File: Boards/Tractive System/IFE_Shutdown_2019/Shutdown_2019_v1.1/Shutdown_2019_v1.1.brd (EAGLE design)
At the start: 88.9 x 76.2 mm, 195 parts, among them Q1 DMN6140L-7, Q10 DMN6140L-7, Q11 DMP3099L-7, Q12 IRLML6346PBF, Q13 IRLML6346PBF, Q14 IRLML6346PBF, Q15 DMP3099L-7, Q16 DMN6140L-7, Q17 IRLML6346PBF, Q18 DMN6140L-7, Q2 DMN6140L-7, Q20 DMN6140L-7, Q21 DMN6140L-7, Q3 DMN6140L-7, Q4 DMN6140L-7, Q5 DMN6140L-7, Q6 DMP3099L-7, Q7 DMN6140L-7, Q9 DMN6140L-7, U1 STM32F103CBT6, U2 STM32F103CBT6

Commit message: Still working on 1.1
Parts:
- removed BUZZER: PKMCS0909E4000, MURATA:PKMCS
- added U$6: MAS806Q, MALLORY:MAS806Q
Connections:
- net +12V: now also U$6.POS; no longer BUZZER.P$1
- net N$4: now also U$6.NEG; no longer BUZZER.P$2
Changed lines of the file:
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@@
 <?xml version="1.0" encoding="utf-8"?>
 <!DOCTYPE eagle SYSTEM "eagle.dtd">
-<eagle version="9.2.2">
+<eagle version="9.1.2">
 <drawing>
 <settings>
@@
 <attribute name="NAME" x="22.225" y="26.797" size="0.8128" layer="25" rot="R180"/>
 </element>
-<element name="BUZZER" library="MURATA" package="PKMCS" value="PKMCS0909E4000" x="94.742" y="18.796" smashed="yes" rot="R90">
-<attribute name="NAME" x="89.789" y="14.224" size="0.8128" layer="25" rot="R90"/>
-</element>
 <element name="U$1" library="KEMET" package="DPDT_2.54" value="EC2" x="16.51" y="67.31" smashed="yes" rot="R90">
 <attribute name="NAME" x="20.574" y="74.676" size="0.8128" layer="25" rot="R270"/>
@@
 <attribute name="NAME" x="40.894" y="74.676" size="0.8128" layer="25" rot="R270"/>
 </element>
+<element name="U$6" library="MALLORY" package="MAS806Q" value="MAS806Q" x="104.902" y="29.972" rot="R180"/>
 </elements>
 <signals>
@@
 <wire x1="14.7546" y1="64.77" x2="17.46" y2="64.77" width="0.4064" layer="16"/>
 <wire x1="15.748" y1="45.5372" x2="15.748" y2="49.53" width="0.4064" layer="1"/>
-<contactref element="BUZZER" pad="P$1"/>
 <contactref element="U$1" pad="$P5"/>
 <contactref element="U$2" pad="$P5"/>
 <contactref element="U$3" pad="$P5"/>
-<wire x1="94.742" y1="14.296" x2="16.256" y2="45.0292" width="0" layer="19" extent="1-1"/>
-<wire x1="19.05" y1="71.12" x2="94.742" y2="14.296" width="0" layer="19" extent="1-1"/>
-<wire x1="29.21" y1="71.12" x2="19.05" y2="71.12" width="0" layer="19" extent="1-1"/>
-<wire x1="39.37" y1="71.12" x2="29.21" y2="71.12" width="0" layer="19" extent="1-1"/>
+<contactref element="U$6" pad="POS"/>
+<wire x1="37.78" y1="67.63" x2="39.37" y2="71.12" width="0" layer="19" extent="16-16"/>
+<wire x1="29.21" y1="71.12" x2="27.62" y2="67.63" width="0" layer="19" extent="16-16"/>
+<wire x1="19.05" y1="71.12" x2="17.46" y2="67.63" width="0" layer="19" extent="16-16"/>
+<wire x1="104.902" y1="36.972" x2="16.256" y2="45.0292" width="0" layer="19" extent="1-1"/>
 </signal>
 <signal name="FAULT_BSPD_STAT">
@@
 </signal>
 <signal name="N$4">
-<contactref element="BUZZER" pad="P$2"/>
 <contactref element="Q4" pad="3"/>
-<wire x1="94.742" y1="23.296" x2="86.36" y2="16.34" width="0" layer="19" extent="1-1"/>
+<contactref element="U$6" pad="NEG"/>
+<wire x1="104.902" y1="22.972" x2="86.36" y2="16.34" width="0" layer="19" extent="1-1"/>
 </signal>
 <signal name="ANALOG_5V" class="1">

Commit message: Finished pre review Safety V1.1
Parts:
- removed CURRENT_SENSOR_SUPPLY, PWR: MINIFIT_JR_5566-02, Display_Custom:MINIFIT_JR_5566-02
- removed DRIVERS, FAULT_INPUT, HALL_SENSE, THROTTLE, TSAL_EN: MINIFIT_JR_5566-04, Display_Custom:MINIFIT_JR_5566-04
- removed Q17: IRLML6346PBF, TRANS:SOT23
- removed R6: 3.6k, rcl:R0603
- added C40, C41: 0.001u, rcl:C0805
- added C42, C43, C44, C45, C46: 0.1u, resistor:C0603
- added CURRENT_SENSE_SUPPLY, POWER, POWER_ANALOG, SOFT_FAULT_STAT: 505575-02, MOLEX:505575-02
- added FAULT_IN, LIGHTING, THROTTLE_TC: 505575-05, MOLEX:505575-05
- added FAULT_STAT: 505575-03, MOLEX:505575-03
- added HALL_SENSOR_INPUT: 505575-04, MOLEX:505575-04
- added Q8: DMN6140L-7, TRANS:SOT23
- added R10, R78: 10, rcl:R0603
- added R45, R75, R79, R80: 10k, rcl:R0603
- added R76, R81: 15k, rcl:R0603
- added R77, R82: 1k, rcl:R0603
- added R83: 10k, resistor:R0603
- added U$13, U$15: LMV321L, STM:SOT23-5
- added U$14, U$19: BZT52C5V6, DIODES_INC:SOD-123
- added U$27: SN74LVC1G08, TEXAS_INSTRUMENTS:SOT23-5
- added U$28: CD4072BM96, TEXAS_INSTRUMENTS:SOIC8
- added U$30, U$31: TS881, STM:SOT23-5
- AIR, CAN, ENABLE: value MINIFIT_JR_5566-02 -> 505575-02; device Display_Custom:MINIFIT_JR_5566-02 -> MOLEX:505575-02
- Q13: value IRLML6346PBF -> DMN6140L-7
- R3: value 3.6k -> 10k; device rcl:R0603 -> resistor:R0603
- U$7: value DNBT8105 -> SN74LVC1G04DBVR; device DIODES_INC:SOT23-3 -> Display_Custom:SOT23-5L
- U$8: value DNBT8105 -> 0805_INDUCTOR; device DIODES_INC:SOT23-3 -> Display_Custom:L0805
- moved U$8 275.9 mm to (-52.8, -227.3), turned to 0 degrees
- moved R3 274.2 mm to (-53.6, -222.5)
- moved Q13 272.2 mm to (-47.0, -216.4), turned to 0 degrees
- moved U$7 271.9 mm to (-52.6, -216.7), turned to 0 degrees
- moved Q4 57.5 mm to (45.7, 55.9)
- moved C11 47.2 mm to (99.3, 82.8), turned to 90 degrees
- moved C14 47.2 mm to (99.3, 87.9), turned to 270 degrees
- moved FUSE 45.0 mm to (80.3, 93.0)
- moved D11 44.3 mm to (97.3, 82.8), turned to 0 degrees
- moved D12 44.3 mm to (97.3, 87.9), turned to 180 degrees
- moved U$25 43.4 mm to (4.06, 79.8)
- moved C22 43.0 mm to (3.30, 76.2)
- moved R25 42.9 mm to (3.81, 72.9)
- moved R33 42.4 mm to (6.86, 77.5)
- moved R34 42.3 mm to (6.86, 75.2)
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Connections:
- removed net BSPD_OC: Q17.1, U$17.1
- removed net BSPD_SC: Q14.1, U$16.1
- removed net N$15: R3.2, U$8.1
- removed net N$16: R6.2, U$7.1
- removed net TSAL_HV_EN: R3.1, U1.22
- removed net TSAL_LV_EN: R6.1, U1.25
- new net APPS_STAT: SOFT_FAULT_STAT.1
- new net BRAKE_POS: R10.1, THROTTLE_TC.5
- new net BRAKE_POS_F: R75.2, U$13.3, U$13.4
- new net BRAKE_POS_F_3_3: R75.1, R76.2, U1.11
- new net BSPD_BP_OC: U$28.P2, U$31.1
- new net BSPD_BP_SC: U$28.P3, U$30.1
- new net BSPD_COND: Q12.1, R83.2, U$27.4
- new net BSPD_CS_OC: U$17.1, U$28.P4
- new net BSPD_CS_SC: U$16.1, U$28.P5
- new net BSPD_SENSOR_FAULT: Q14.1, U$28.P1
- new net BTSF_STAT: SOFT_FAULT_STAT.2
- new net N$22: R78.2, R79.1, R82.1, U$19.C
- new net N$23: C41.1, R79.2, U$15.1
- new net N$5: R10.2, R45.1, R77.1, U$14.C
- new net N$7: C40.1, R45.2, U$13.1
- new net STEERING_POS: R78.1, THROTTLE_TC.4
- new net STEERING_POS_F: R80.2, U$15.3, U$15.4
- new net STEERING_POS_F_3_3: R80.1, R81.2, U1.12
- net +3V3: now also U$7.5
- net +5V: now also C42.1, C43.1, C44.1, C45.1, C46.1, CURRENT_SENSE_SUPPLY.1, R77.2, R82.2, U$13.5, U$15.5, U$27.5, U$28.P14, U$30.5, U$31.5; no longer CURRENT_SENSOR_SUPPLY.1, TSAL_EN.1
- net AGND: now also POWER_ANALOG.2, U$8.1
- net AIR_IN: now also AIR.2; no longer AIR.1
- net AIR_OUT: now also AIR.1; no longer AIR.2
- net ANALOG_5V: now also POWER_ANALOG.1
- net BRAKE_LIGHT-: now also LIGHTING.4; no longer DRIVERS.1
- net BRAKE_PRESSURE: now also FAULT_IN.4; no longer FAULT_INPUT.4
- net BRAKE_PRESSURE_F: now also U$30.4, U$31.3
- net BSPD_BRAKE_COND: now also U$27.2; no longer Q13.1
- net BSPD_CURR_COND: now also U$27.1; no longer Q12.1
- net CURRENT_SENSE: now also FAULT_IN.5; no longer FAULT_INPUT.2
- net ENABLE_IN: now also ENABLE.2; no longer ENABLE.1
- net ENABLE_OUT: now also ENABLE.1; no longer ENABLE.2
- net FAULT_BMS: now also FAULT_IN.3; no longer FAULT_INPUT.1
- net FAULT_BMS_STAT: now also FAULT_STAT.2
- net FAULT_BMS_STATUS_3_3: now also U1.22; no longer U1.12
- net FAULT_BSPD: no longer Q17.3
- net FAULT_BSPD_STAT: now also FAULT_STAT.1
- net FAULT_IMD: now also FAULT_IN.2; no longer FAULT_INPUT.3
- net FAULT_IMD_STAT: now also FAULT_STAT.3
- net FAULT_RESET: now also FAULT_IN.1; no longer TSAL_EN.4
- net GND: now also C40.2, C41.2, C42.2, C43.2, C44.2, C45.2, C46.2, CURRENT_SENSE_SUPPLY.2, POWER.2, Q12.2, Q8.2, R3.1, R76.1, R81.1, R83.1, U$13.2, U$14.A, U$15.2, U$19.A, U$27.3, U$28.P7, U$30.2, U$31.2, U$7.3; no longer CURRENT_SENSOR_SUPPLY.2, PWR.2, Q17.2, TSAL_EN.3, U$7.2
- net HALL_FL: now also HALL_SENSOR_INPUT.1; no longer HALL_SENSE.1
- net HALL_FR: now also HALL_SENSOR_INPUT.2; no longer HALL_SENSE.3
- net HALL_RL: now also HALL_SENSOR_INPUT.3; no longer HALL_SENSE.2
- net HALL_RR: now also HALL_SENSOR_INPUT.4; no longer HALL_SENSE.4
- net HV_CONNECTED_3_3: now also Q8.1, U$7.2
- net N$9: now also Q13.1, R3.2, U$7.4; no longer Q12.2, Q13.3
- net OC_TH: now also U$31.4
- net PRECHARGE_COMPLETE: now also LIGHTING.5; no longer THROTTLE.3
- net PWR: now also POWER.1; no longer PWR.1
- net SC_TH: now also U$30.3
- net THROTTLE_A: now also THROTTLE_TC.1; no longer THROTTLE.1
- net THROTTLE_B: now also THROTTLE_TC.2; no longer THROTTLE.2
- net THROTTLE_OUT: now also THROTTLE_TC.3; no longer THROTTLE.4
- net TSAL_EN: now also LIGHTING.1; no longer TSAL_EN.2
- net TSAL_HV-: now also LIGHTING.3, Q8.3; no longer DRIVERS.4, U$8.3
- net TSAL_LV-: now also LIGHTING.2, Q13.3; no longer DRIVERS.2, U$7.3
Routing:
- net +5V: track 267.6 -> 0.00 mm, vias 26 -> 0
- net +3V3: track 219.4 -> 0.00 mm, vias 17 -> 0
- net +12V: track 145.6 -> 0.00 mm, vias 4 -> 0
- net FAULT_BSPD_STATUS_3_3: track 70.7 -> 0.00 mm, vias 5 -> 0
- net RTDS_EN: track 62.8 -> 0.00 mm, vias 4 -> 0
- net GND: track 62.7 -> 0.00 mm, vias 128 -> 0
- net FAULT_BMS_STATUS_3_3: track 57.2 -> 0.00 mm, vias 3 -> 0
- net FAULT_IMD_STATUS_3_3: track 48.9 -> 0.00 mm, vias 3 -> 0
- net RTD_EN: track 47.2 -> 0.00 mm, vias 2 -> 0
- net BRAKE_PRESSURE_F_3_3: track 46.3 -> 0.00 mm, vias 4 -> 0
- net HV_CONNECTED_3_3: track 45.8 -> 0.00 mm
- net BTSF_EN: track 44.4 -> 0.00 mm, vias 2 -> 0
- net APPS_EN: track 43.9 -> 0.00 mm
- net FAULT_RESET_F: track 43.5 -> 0.00 mm, vias 3 -> 0
- net AIR_OUT: track 41.3 -> 0.00 mm
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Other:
- board size 88.9 x 76.2 mm -> 101.6 x 101.6 mm
- board text added: "Power"

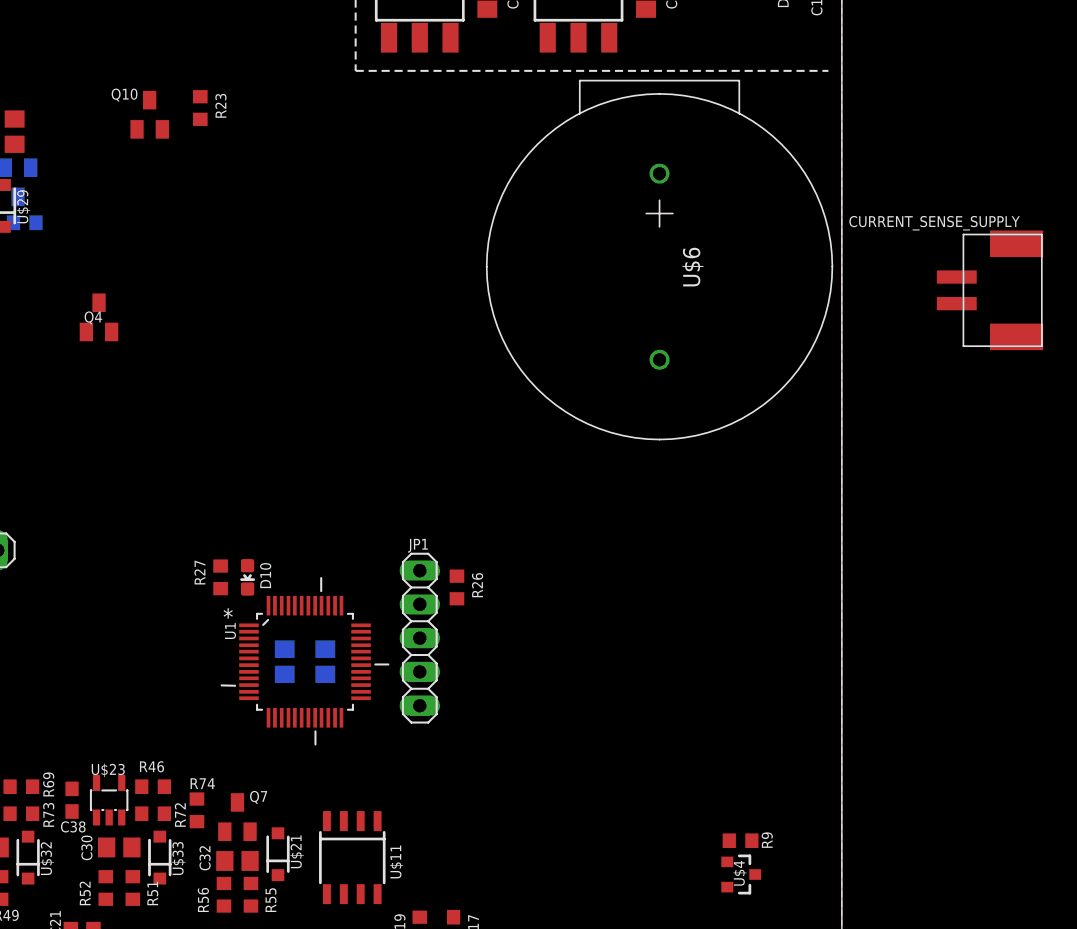
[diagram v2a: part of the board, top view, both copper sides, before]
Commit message: Added TSAL Board
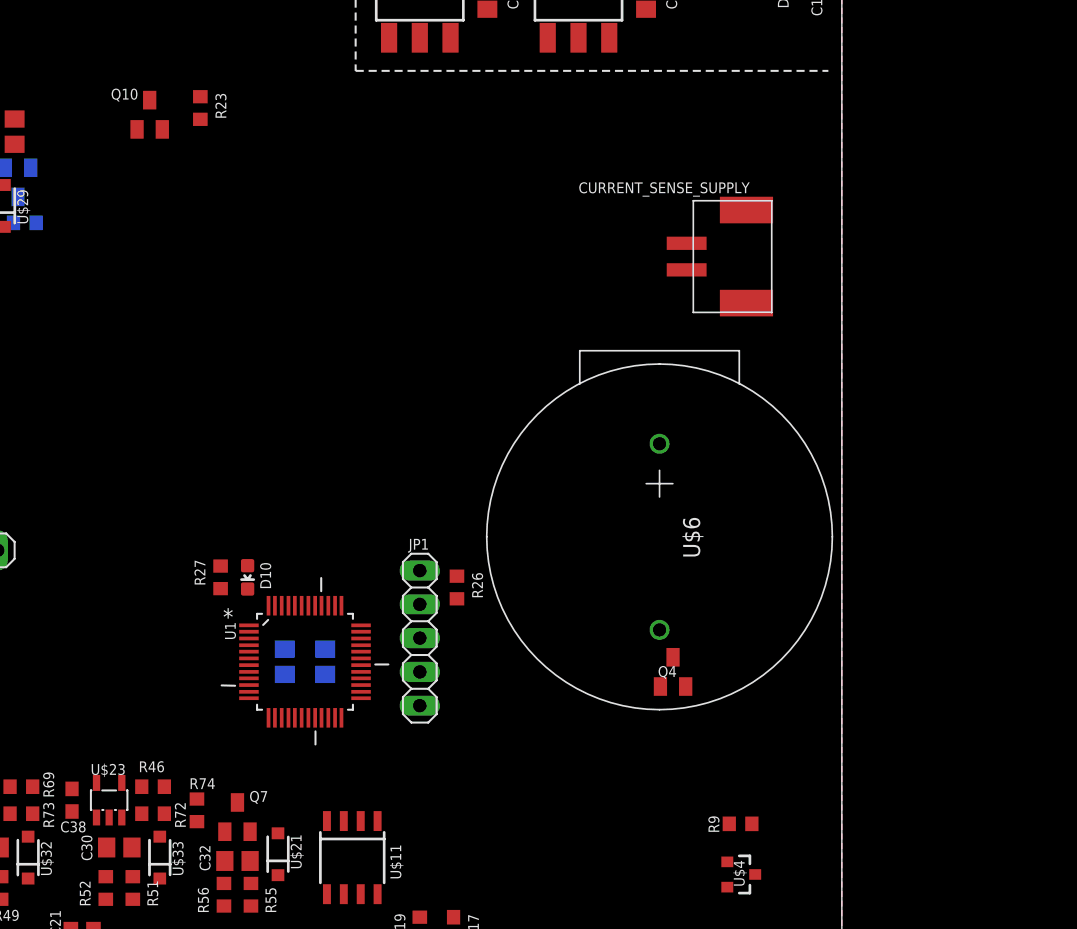
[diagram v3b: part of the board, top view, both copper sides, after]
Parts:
- moved Q4 50.8 mm to (88.9, 29.2)
- moved CURRENT_SENSE_SUPPLY 20.5 mm to (90.4, 60.5)
- moved U$6 20.3 mm to (87.9, 39.4)
- moved R9 1.27 mm to (94.0, 17.8), turned to 180 degrees

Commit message: Ready to route
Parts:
- moved Q13 273.7 mm to (88.3, 21.6)
- moved R3 272.8 mm to (81.3, 14.6)
- moved U$7 270.0 mm to (81.3, 17.8), turned to 270 degrees
- moved C46 268.9 mm to (15.2, 58.4), turned to 270 degrees
- moved Q8 265.1 mm to (83.8, 21.6)
- moved U$8 254.4 mm to (36.8, 10.8), turned to 90 degrees
- moved C44 242.8 mm to (1.27, 44.5), turned to 90 degrees
- moved C45 242.5 mm to (1.27, 39.4), turned to 270 degrees
- moved U$31 237.0 mm to (4.45, 44.5)
- moved R83 231.5 mm to (9.53, 58.4), turned to 90 degrees
- moved U$28 228.8 mm to (5.71, 51.4)
- moved U$27 226.0 mm to (12.7, 58.4)
- moved U$30 224.7 mm to (4.45, 39.4)
- moved C43 184.7 mm to (56.5, 21.0), turned to 90 degrees
- moved C42 178.3 mm to (50.8, 21.0), turned to 90 degrees
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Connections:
- net AGND: now also C21.2
- net BRAKE_POS: now also THROTTLE_TC.4; no longer THROTTLE_TC.5
- net CANH: now also CAN.1; no longer CAN.2
- net CANL: now also CAN.2; no longer CAN.1
- net GND: no longer C21.2
- net STEERING_POS: now also THROTTLE_TC.3; no longer THROTTLE_TC.4
- net THROTTLE_OUT: now also THROTTLE_TC.5; no longer THROTTLE_TC.3
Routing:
- removed copper zone on layer 1, net GND
- removed copper zone on layer 16, net GND
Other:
- board size 101.6 x 101.6 mm -> 99.1 x 91.4 mm
- board text removed: "Power"

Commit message: finished safety v1.1 layout
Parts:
- moved Q4 36.0 mm to (71.8, 56.5)
- moved C45 6.99 mm to (8.26, 39.4)
- moved U$17 6.35 mm to (4.45, 39.4)
- moved U$30 6.35 mm to (10.8, 39.4)
- moved C27 5.71 mm to (1.91, 39.4)
- moved U$38 3.86 mm to (19.7, 12.1)
- moved C36 3.86 mm to (9.53, 15.2)
- moved R63 3.86 mm to (9.53, 11.4)
- moved U$39 3.86 mm to (12.1, 12.1)
- moved R64 3.86 mm to (6.99, 14.6)
- moved R68 3.86 mm to (6.99, 11.4)
- moved C34 3.86 mm to (24.8, 15.2)
- moved C35 3.86 mm to (17.1, 15.2)
- moved R59 3.86 mm to (24.8, 11.4)
- moved R60 3.86 mm to (22.2, 14.6)
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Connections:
- removed net APPS_STAT: SOFT_FAULT_STAT.1
- removed net BTSF_STAT: SOFT_FAULT_STAT.2
- net APPS_EN: now also SOFT_FAULT_STAT.1
- net BSPD_BP_SC: now also U$28.P4; no longer U$28.P3
- net BSPD_CS_OC: now also U$28.P3; no longer U$28.P4
- net BTSF_EN: now also SOFT_FAULT_STAT.2
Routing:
- net +3V3: track 0.00 -> 319.1 mm, vias 0 -> 23
- net +5V: track 0.00 -> 317.3 mm, vias 0 -> 35
- net +12V: track 0.00 -> 218.8 mm, vias 0 -> 7
- net PRECHARGE_COMPLETE_3_3: track 0.00 -> 70.5 mm, vias 0 -> 6
- net HV_CONNECTED_3_3: track 0.00 -> 64.3 mm, vias 0 -> 4
- net FAULT_BSPD_STAT: track 0.00 -> 64.2 mm, vias 0 -> 3
- net THROTTLE_A_F_3_3: track 0.00 -> 54.1 mm, vias 0 -> 2
- net BRAKE_LIGHT_EN: track 0.00 -> 54.0 mm, vias 0 -> 4
- net FAULT_BMS_STAT: track 0.00 -> 50.1 mm, vias 0 -> 2
- net THROTTLE_B_F_3_3: track 0.00 -> 49.4 mm, vias 0 -> 2
- net FAULT_BSPD_STATUS_3_3: track 0.00 -> 48.5 mm, vias 0 -> 4
- net SDA_TC: track 0.00 -> 47.0 mm, vias 0 -> 5
- net THROTTLE_A_F: track 0.00 -> 46.5 mm, vias 0 -> 2
- net FAULT_RESET_F: track 0.00 -> 46.0 mm, vias 0 -> 7
- net SPI1_MOSI: track 0.00 -> 46.0 mm
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- added copper zone on layer 1, net AGND
- added copper zone on layer 16, net AGND
- added copper zone on layer 1, net GND
- added copper zone on layer 16, net GND
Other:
- board text added: "Apollo 2019 V1.1"
- board text removed: "Apollo 2019 V1.0"
